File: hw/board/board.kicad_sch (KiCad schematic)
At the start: 12 parts, among them J2 Conn_ARM_JTAG_SWD_10, U2 W25Q128JVSIQTR, U6 XC7A35T-FTG256

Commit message: Updated silkscreen
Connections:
- net GND: now also U6.L15 (IO_L3P_T0_DQS_PUDC_B_14)
- no-connect marks 119 -> 118
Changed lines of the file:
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@@
-	)
-	(no_connect
-		(at 334.01 180.34)
 	)
 	(no_connect
@@
 	(wire
 		(pts
+			(xy 330.2 180.34) (xy 330.2 182.88)
+		)
+		(stroke
+			(width 0)
+			(type default)
+		)
+	)
+	(wire
+		(pts
 			(xy 425.45 144.78) (xy 425.45 147.32)
 		)
@@
 		(pts
 			(xy 354.33 144.78) (xy 356.87 144.78)
+		)
+		(stroke
+			(width 0)
+			(type default)
+		)
+	)
+	(wire
+		(pts
+			(xy 334.01 180.34) (xy 330.2 180.34)
 		)
 		(stroke
@@
 					(unit 1)
 				)
+			)
+		)
+	)
+	(symbol
+		(lib_id "power:GND")
+		(at 330.2 182.88 0)
+		(unit 1)
+		(exclude_from_sim no)
+		(in_bom yes)
+		(on_board yes)
+		(dnp no)
+		(fields_autoplaced yes)
+		(property "Reference" "#PWR052"
+			(at 330.2 189.23 0)
+			(effects
+				(font
+					(size 1.27 1.27)
+				)
+				(hide yes)
+			)
+		)
+		(property "Value" "GND"
+			(at 330.2 187.96 0)
+			(effects
+				(font
+					(size 1.27 1.27)
+				)
+			)
+		)
+		(property "Footprint" ""
+			(at 330.2 182.88 0)
+			(effects
+				(font
+					(size 1.27 1.27)
+				)
+				(hide yes)
+			)
+		)
+		(property "Datasheet" ""
+			(at 330.2 182.88 0)
+			(effects
+				(font
+					(size 1.27 1.27)
+				)
+				(hide yes)
+			)
+		)
+		(property "Description" "Power symbol creates a global label with name \"GND\" , ground"
+			(at 330.2 182.88 0)
+			(effects
+				(font
+					(size 1.27 1.27)
+				)
+				(hide yes)
+			)
+		)
+		(pin "1"
+		)
+		(instances
+			(project ""
+				(path "/0e384709-6bce-4dbf-a0e0-550e970390f4"
+					(reference "#PWR052")
+					(unit 1)
+				)

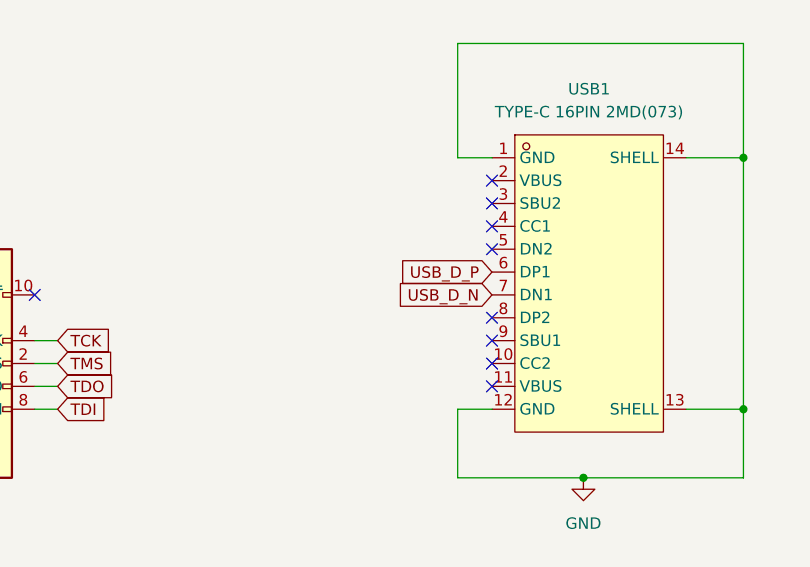
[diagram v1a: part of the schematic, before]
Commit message: Fixed USB C port
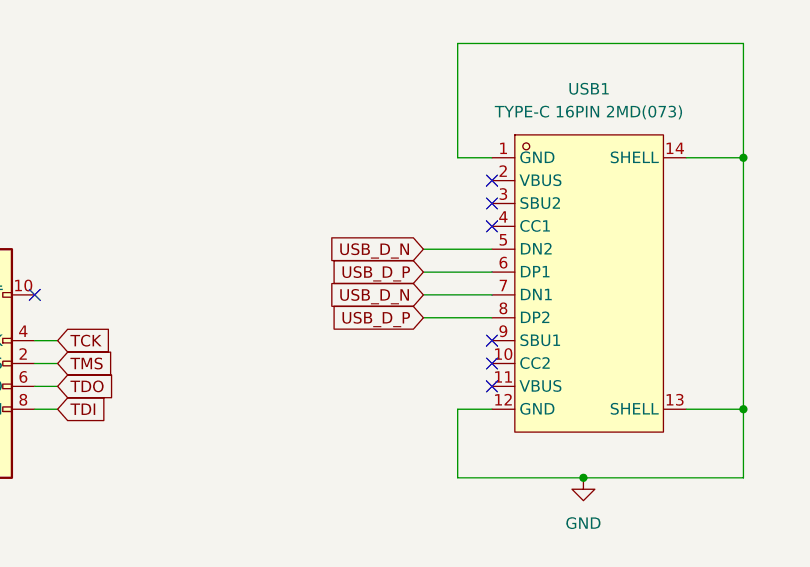
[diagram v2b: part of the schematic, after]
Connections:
- net USB_D_N: now also USB1.5 (DN2)
- net USB_D_P: now also USB1.8 (DP2)
- no-connect marks 118 -> 116
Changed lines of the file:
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@@
-	)
-	(no_connect
-		(at 353.06 58.42)
 	)
 	(no_connect
@@
 	)
 	(no_connect
-		(at 353.06 50.8)
-	)
-	(no_connect
 		(at 143.51 228.6)
 	)
@@
 	(wire
 		(pts
+			(xy 345.44 50.8) (xy 353.06 50.8)
+		)
+		(stroke
+			(width 0)
+			(type default)
+		)
+	)
+	(wire
+		(pts
 			(xy 411.48 101.6) (xy 401.32 101.6)
 		)
@@
 	(wire
 		(pts
+			(xy 345.44 58.42) (xy 353.06 58.42)
+		)
+		(stroke
+			(width 0)
+			(type default)
+		)
+	)
+	(wire
+		(pts
 			(xy 353.06 68.58) (xy 349.25 68.58)
 		)
@@
 	(wire
 		(pts
+			(xy 345.44 53.34) (xy 353.06 53.34)
+		)
+		(stroke
+			(width 0)
+			(type default)
+		)
+	)
+	(wire
+		(pts
 			(xy 288.29 80.01) (xy 288.29 81.28)
 		)
@@
 	(wire
 		(pts
+			(xy 345.44 55.88) (xy 353.06 55.88)
+		)
+		(stroke
+			(width 0)
+			(type default)
+		)
+	)
+	(wire
+		(pts
 			(xy 349.25 40.64) (xy 353.06 40.64)
 		)
@@
 		)
 	)
+	(global_label "USB_D_P"
+		(shape input)
+		(at 345.44 53.34 180)
+		(fields_autoplaced yes)
+		(effects
+			(font
+				(size 1.27 1.27)
+			)
+			(justify right)
+		)
+		(property "Intersheetrefs" "${INTERSHEET_REFS}"
+			(at 334.1696 53.34 0)
+			(effects
+				(font
+					(size 1.27 1.27)
+				)
+				(justify right)
+				(hide yes)
+			)
+		)
+	)
 	(global_label "S_{out}1_N"
 		(shape output)
@@
 	(global_label "USB_D_N"
 		(shape input)
-		(at 353.06 55.88 180)
+		(at 345.44 55.88 180)
 		(fields_autoplaced yes)
 		(effects
@@
 		)
 		(property "Intersheetrefs" "${INTERSHEET_REFS}"
-			(at 341.7291 55.88 0)
+			(at 334.1091 55.88 0)
 			(effects
 				(font
@@
 		)
 	)
+	(global_label "D_{in}7_P"
+		(shape input)
+		(at 435.61 256.54 0)
+		(fields_autoplaced yes)
+		(effects
+			(font
+				(size 1.27 1.27)
+			)
+			(justify left)
+		)
+		(property "Intersheetrefs" "${INTERSHEET_REFS}"
+			(at 444.7153 256.54 0)
+			(effects
+				(font
+					(size 1.27 1.27)
+				)
+				(justify left)
+				(hide yes)
+			)
+		)
+	)
+	(global_label "D_{in}2_P"
+		(shape input)
+		(at 143.51 281.94 0)
+		(fields_autoplaced yes)
+		(effects
+			(font
+				(size 1.27 1.27)
+			)
+			(justify left)
+		)
+		(property "Intersheetrefs" "${INTERSHEET_REFS}"
+			(at 152.6153 281.94 0)
+			(effects
+				(font
+					(size 1.27 1.27)
+				)
+				(justify left)
+				(hide yes)
+			)
+		)
+	)
+	(global_label "S_{in}2_P"
+		(shape input)
+		(at 143.51 276.86 0)
+		(fields_autoplaced yes)
+		(effects
+			(font
+				(size 1.27 1.27)
+			)
+			(justify left)
+		)
+		(property "Intersheetrefs" "${INTERSHEET_REFS}"
+			(at 152.5548 276.86 0)
+			(effects
+				(font
+					(size 1.27 1.27)
+				)
+				(justify left)
+				(hide yes)
+			)
+		)
+	)
+	(global_label "FLASH_SCK"
+		(shape input)
+		(at 381 106.68 0)
+		(fields_autoplaced yes)
+		(effects
+			(font
+				(size 1.27 1.27)
+			)
+			(justify left)
+		)
+		(property "Intersheetrefs" "${INTERSHEET_REFS}"
+			(at 394.4476 106.68 0)
+			(effects
+				(font
+					(size 1.27 1.27)
+				)
+				(justify left)
+				(hide yes)
+			)
+		)
+	)
+	(global_label "CCLK"
+		(shape input)
+		(at 196.85 64.77 0)
+		(fields_autoplaced yes)
+		(effects
+			(font
+				(size 1.27 1.27)
+			)
+			(justify left)
+		)
+		(property "Intersheetrefs" "${INTERSHEET_REFS}"
+			(at 204.6733 64.77 0)
+			(effects
+				(font
+					(size 1.27 1.27)
+				)
+				(justify left)
+				(hide yes)
+			)
+		)
+	)
 	(global_label "USB_D_P"
 		(shape input)
-		(at 353.06 53.34 180)
+		(at 345.44 58.42 180)
 		(fields_autoplaced yes)
 		(effects
@@
 		)
 		(property "Intersheetrefs" "${INTERSHEET_REFS}"
-			(at 341.7896 53.34 0)
+			(at 334.1696 58.42 0)
 			(effects
 				(font
@@
 		)
 	)
-	(global_label "D_{in}7_P"
-		(shape input)
-		(at 435.61 256.54 0)
-		(fields_autoplaced yes)
-		(effects
-			(font
-				(size 1.27 1.27)
-			)
-			(justify left)
-		)
-		(property "Intersheetrefs" "${INTERSHEET_REFS}"
-			(at 444.7153 256.54 0)
-			(effects
-				(font
-					(size 1.27 1.27)
-				)
-				(justify left)
-				(hide yes)
-			)
-		)
-	)
-	(global_label "D_{in}2_P"
-		(shape input)
-		(at 143.51 281.94 0)
-		(fields_autoplaced yes)
-		(effects
-			(font
-				(size 1.27 1.27)
-			)
-			(justify left)
-		)
-		(property "Intersheetrefs" "${INTERSHEET_REFS}"
-			(at 152.6153 281.94 0)
-			(effects
-				(font
-					(size 1.27 1.27)
-				)
-				(justify left)
-				(hide yes)
-			)
-		)
-	)
-	(global_label "S_{in}2_P"
-		(shape input)
-		(at 143.51 276.86 0)
-		(fields_autoplaced yes)
-		(effects
-			(font
-				(size 1.27 1.27)
-			)
-			(justify left)
-		)
-		(property "Intersheetrefs" "${INTERSHEET_REFS}"
-			(at 152.5548 276.86 0)
-			(effects
-				(font
-					(size 1.27 1.27)
-				)
-				(justify left)
-				(hide yes)
-			)
-		)
-	)
-	(global_label "FLASH_SCK"
-		(shape input)
-		(at 381 106.68 0)
-		(fields_autoplaced yes)
-		(effects
-			(font
-				(size 1.27 1.27)
-			)
-			(justify left)
-		)
-		(property "Intersheetrefs" "${INTERSHEET_REFS}"
-			(at 394.4476 106.68 0)
-			(effects
-				(font
-					(size 1.27 1.27)
-				)
-				(justify left)
-				(hide yes)
-			)
-		)
-	)
-	(global_label "CCLK"
-		(shape input)
-		(at 196.85 64.77 0)
-		(fields_autoplaced yes)
-		(effects
-			(font
-				(size 1.27 1.27)
-			)
-			(justify left)
-		)
-		(property "Intersheetrefs" "${INTERSHEET_REFS}"
-			(at 204.6733 64.77 0)
-			(effects
-				(font
-					(size 1.27 1.27)
-				)
-				(justify left)
-				(hide yes)
-			)
-		)
-	)
 	(global_label "S_{out}3_P"
 		(shape output)
@@
 				(hide yes)
 			)
+		)
+	)
+	(global_label "USB_D_N"
+		(shape input)
+		(at 345.44 50.8 180)
+		(fields_autoplaced yes)
+		(effects
+			(font
+				(size 1.27 1.27)
+			)
+			(justify right)
+		)
+		(property "Intersheetrefs" "${INTERSHEET_REFS}"
+			(at 334.1091 50.8 0)
+			(effects
+				(font
+					(size 1.27 1.27)
+				)
+				(justify right)
+				(hide yes)
+			)

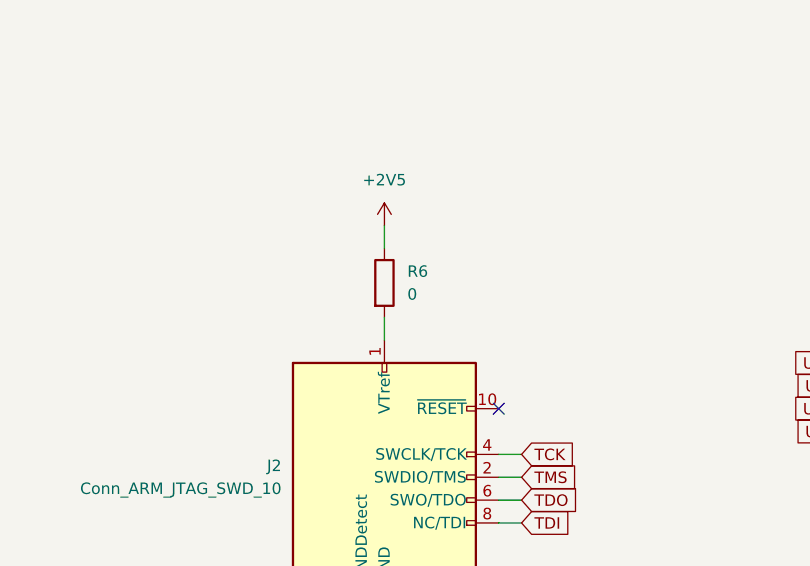
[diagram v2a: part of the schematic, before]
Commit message: Removed unused 0 ohm resistor, add ground vias
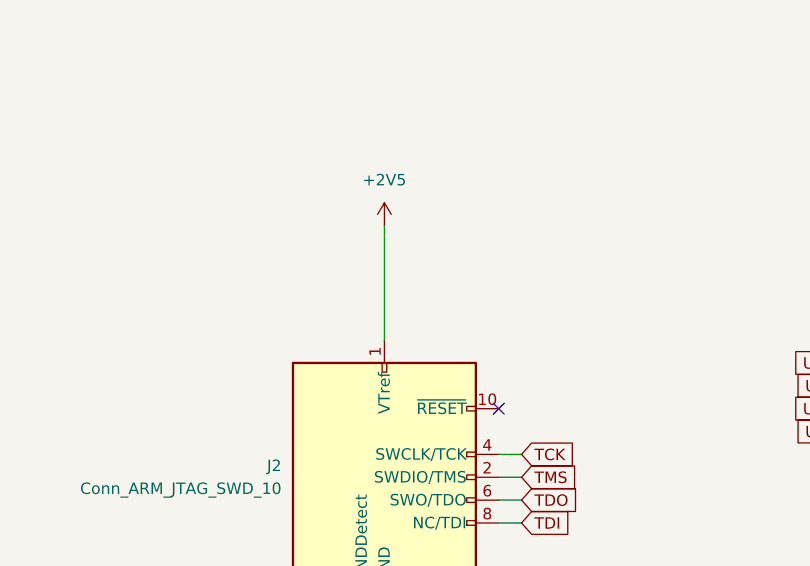
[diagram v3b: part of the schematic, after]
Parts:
- removed R6: 0, Resistor_SMD:R_0805_2012Metric, symbol Device:R
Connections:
- net +2V5: now also J2.1 (VTref)
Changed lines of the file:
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@@
 	(wire
 		(pts
-			(xy 289.56 35.56) (xy 289.56 38.1)
+			(xy 289.56 35.56) (xy 289.56 48.26)
 		)
 		(stroke
@@
 	(wire
 		(pts
-			(xy 289.56 45.72) (xy 289.56 48.26)
-		)
-		(stroke
-			(width 0)
-			(type default)
-		)
-	)
-	(wire
-		(pts
 			(xy 120.65 144.78) (xy 120.65 147.32)
 		)
@@
 					(unit 1)
 				)
-			)
-		)
-	)
-	(symbol
-		(lib_id "Device:R")
-		(at 289.56 41.91 0)
-		(unit 1)
-		(exclude_from_sim no)
-		(in_bom yes)
-		(on_board yes)
-		(dnp no)
-		(fields_autoplaced yes)
-		(property "Reference" "R6"
-			(at 292.1 40.6399 0)
-			(effects
-				(font
-					(size 1.27 1.27)
-				)
-				(justify left)
-			)
-		)
-		(property "Value" "0"
-			(at 292.1 43.1799 0)
-			(effects
-				(font
-					(size 1.27 1.27)
-				)
-				(justify left)
-			)
-		)
-		(property "Footprint" "Resistor_SMD:R_0805_2012Metric"
-			(at 287.782 41.91 90)
-			(effects
-				(font
-					(size 1.27 1.27)
-				)
-				(hide yes)
-			)
-		)
-		(property "Datasheet" "~"
-			(at 289.56 41.91 0)
-			(effects
-				(font
-					(size 1.27 1.27)
-				)
-				(hide yes)
-			)
-		)
-		(property "Description" "Resistor"
-			(at 289.56 41.91 0)
-			(effects
-				(font
-					(size 1.27 1.27)
-				)
-				(hide yes)
-			)
-		)
-		(pin "1"
-		)
-		(pin "2"
-		)
-		(instances
-			(project "board"
-				(path "/0e384709-6bce-4dbf-a0e0-550e970390f4"
-					(reference "R6")
-					(unit 1)
-				)

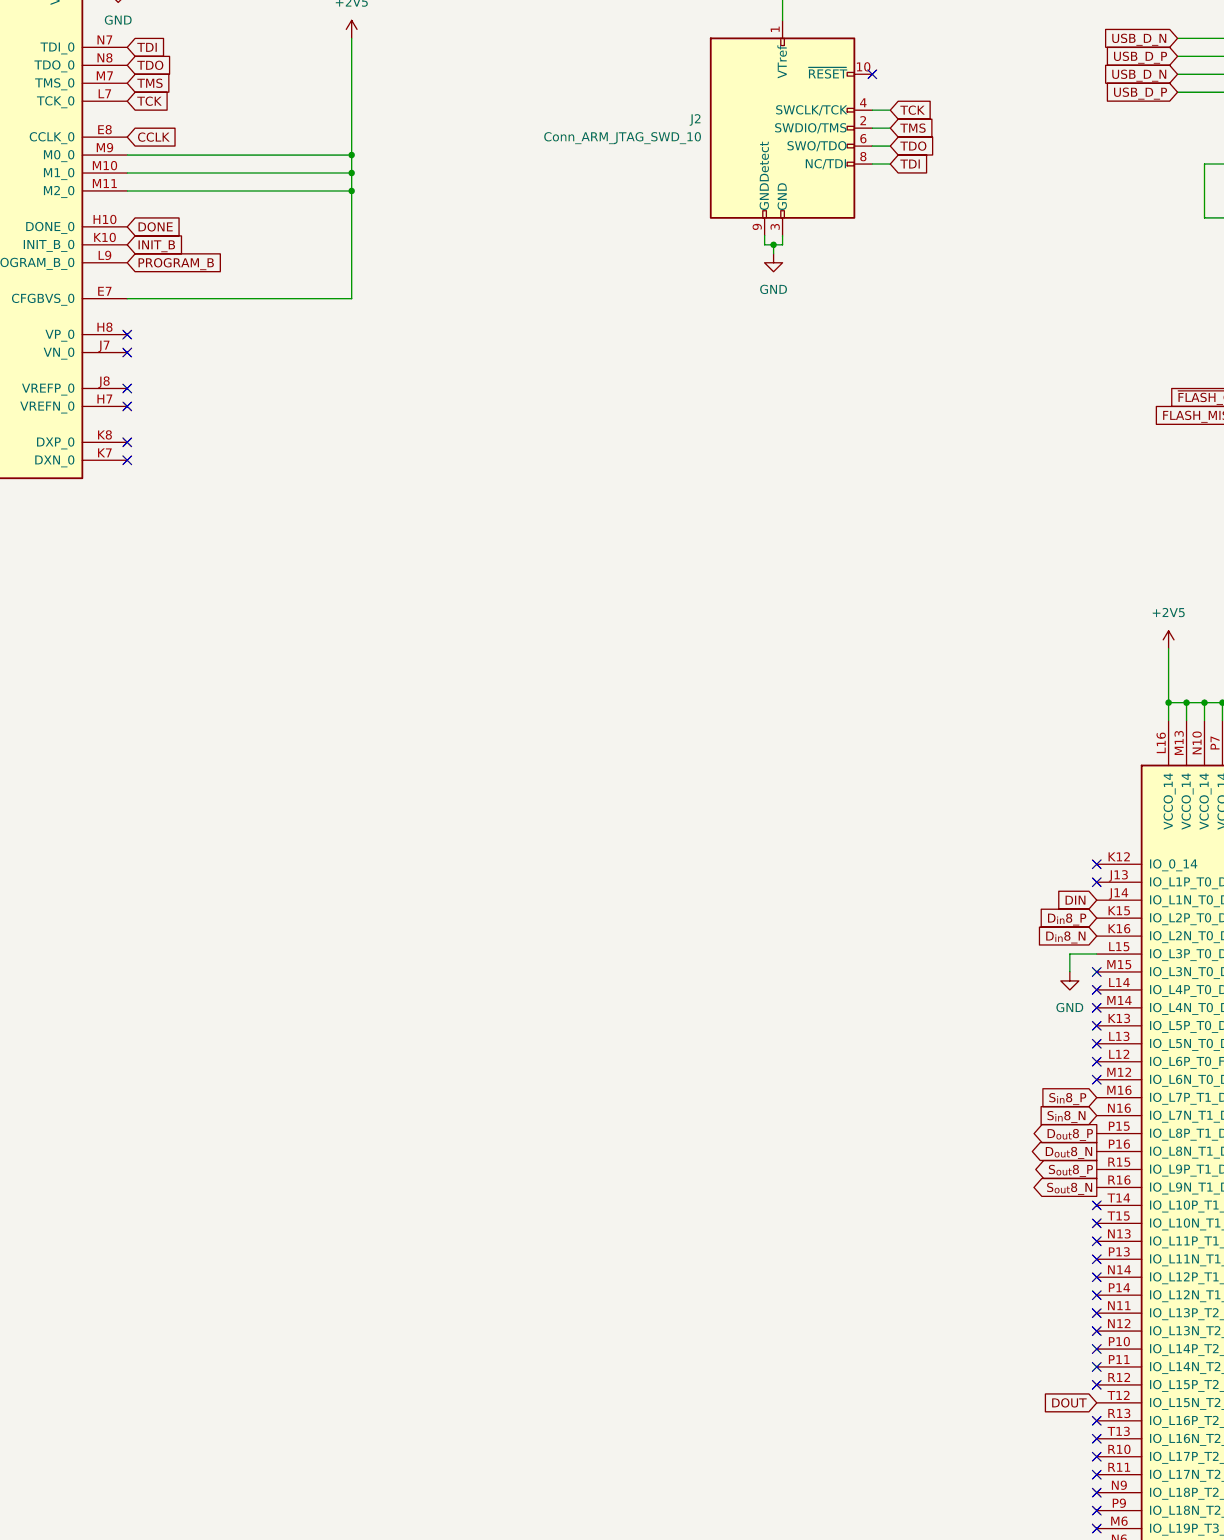
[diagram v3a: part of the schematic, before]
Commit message: Updated net names for SPI bitstream upload
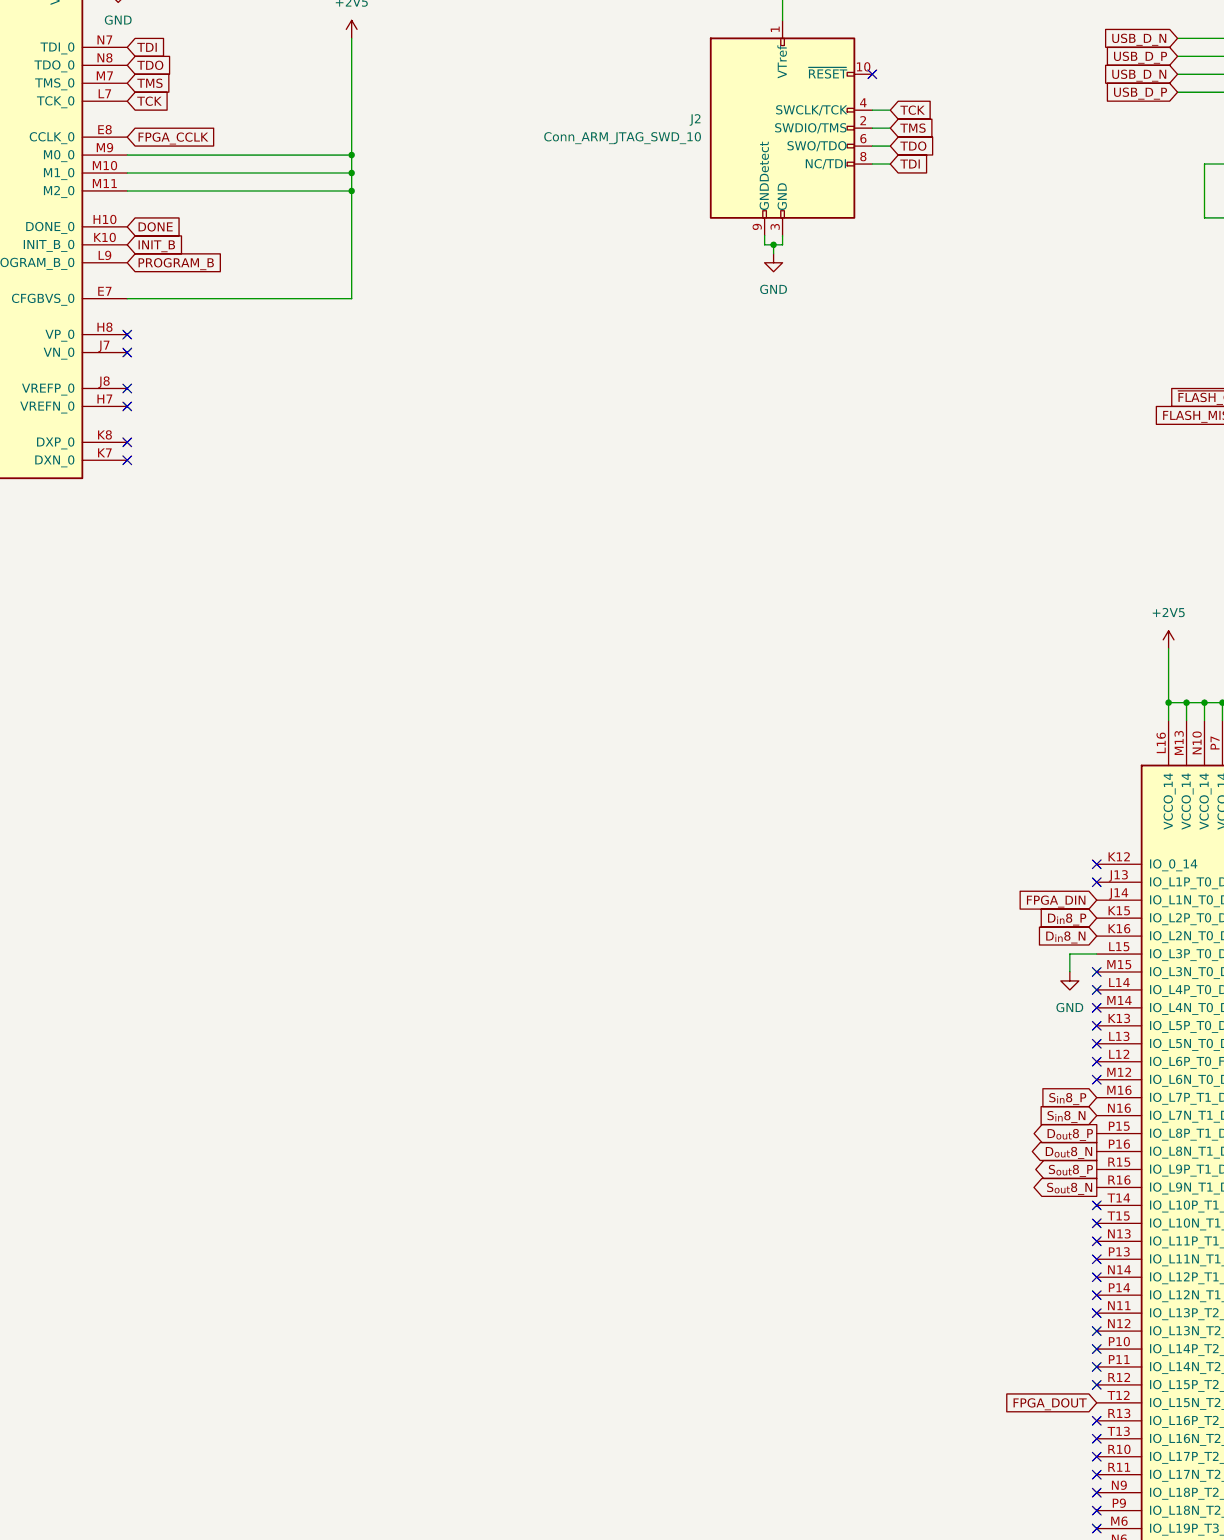
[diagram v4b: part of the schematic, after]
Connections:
- net CCLK renamed FPGA_CCLK
- net DIN renamed FPGA_DIN
- net DOUT renamed FPGA_DOUT
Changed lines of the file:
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@@
 		)
 	)
-	(global_label "DOUT"
+	(global_label "FPGA_DOUT"
 		(shape input)
 		(at 334.01 243.84 180)
@@
 		)
 		(property "Intersheetrefs" "${INTERSHEET_REFS}"
-			(at 326.1262 243.84 0)
+			(at 320.4414 243.84 0)
 			(effects
 				(font
@@
 		)
 	)
-	(global_label "DIN"
+	(global_label "FPGA_DIN"
 		(shape input)
 		(at 334.01 172.72 180)
@@
 		)
 		(property "Intersheetrefs" "${INTERSHEET_REFS}"
-			(at 327.8195 172.72 0)
+			(at 322.1347 172.72 0)
 			(effects
 				(font
@@
 		)
 	)
-	(global_label "CCLK"
+	(global_label "FPGA_CCLK"
 		(shape input)
 		(at 196.85 64.77 0)
@@
 		)
 		(property "Intersheetrefs" "${INTERSHEET_REFS}"
-			(at 204.6733 64.77 0)
-			(effects
-				(font
+			(at 210.3581 64.77 0)
+			(effects
+				(font
